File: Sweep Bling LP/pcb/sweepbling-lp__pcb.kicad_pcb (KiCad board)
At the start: 2 copper layers, 216.9 x 86.9 mm, 59 parts, among them SW1 SW_Push, SW10 SW_Push, SW10_r1 SW_Push, SW11 SW_Push, SW11_r1 SW_Push, SW12 SW_Push, SW12_r1 SW_Push, SW13 SW_Push, SW13_r1 SW_Push, SW14 SW_Push, SW14_r1 SW_Push, SW15 SW_Push, SW15_r1 SW_Push, SW16 SW_Push, SW16_r1 SW_Push, SW17 SW_Push, SW17_r1 SW_Push, SW1_r1 SW_Push, SW2 SW_Push, SW2_r1 SW_Push, SW3 SW_Push, SW3_r1 SW_Push, SW4 SW_Push, SW4_r1 SW_Push, SW5 SW_Push, SW5_r1 SW_Push, SW6 SW_Push, SW6_r1 SW_Push, SW7 SW_Push, SW7_r1 SW_Push, SW8 SW_Push, SW8_r1 SW_Push, SW9 SW_Push, SW9_r1 SW_Push, U1 ProMicro-kbd, U2 ProMicro-kbd

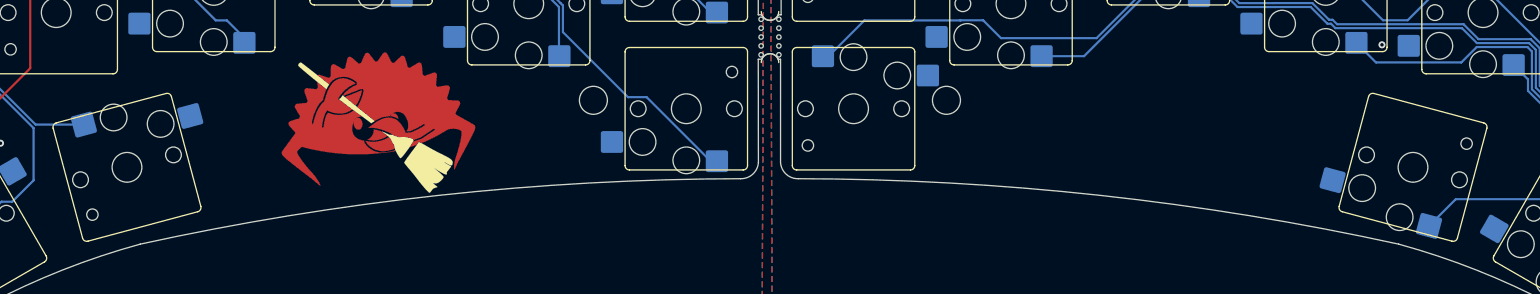
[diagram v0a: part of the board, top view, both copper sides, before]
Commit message: remove crab logo
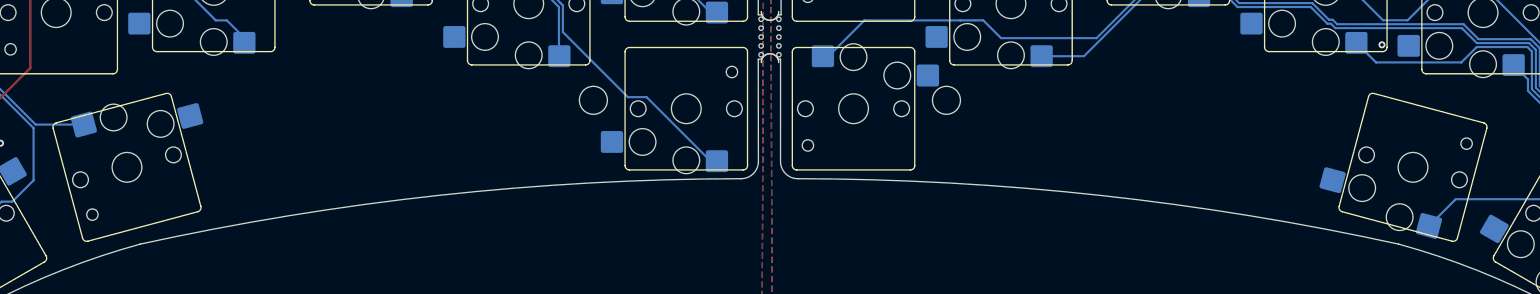
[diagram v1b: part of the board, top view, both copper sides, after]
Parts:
- removed SweepLogo: LOGO, Kailh:ferris_broom

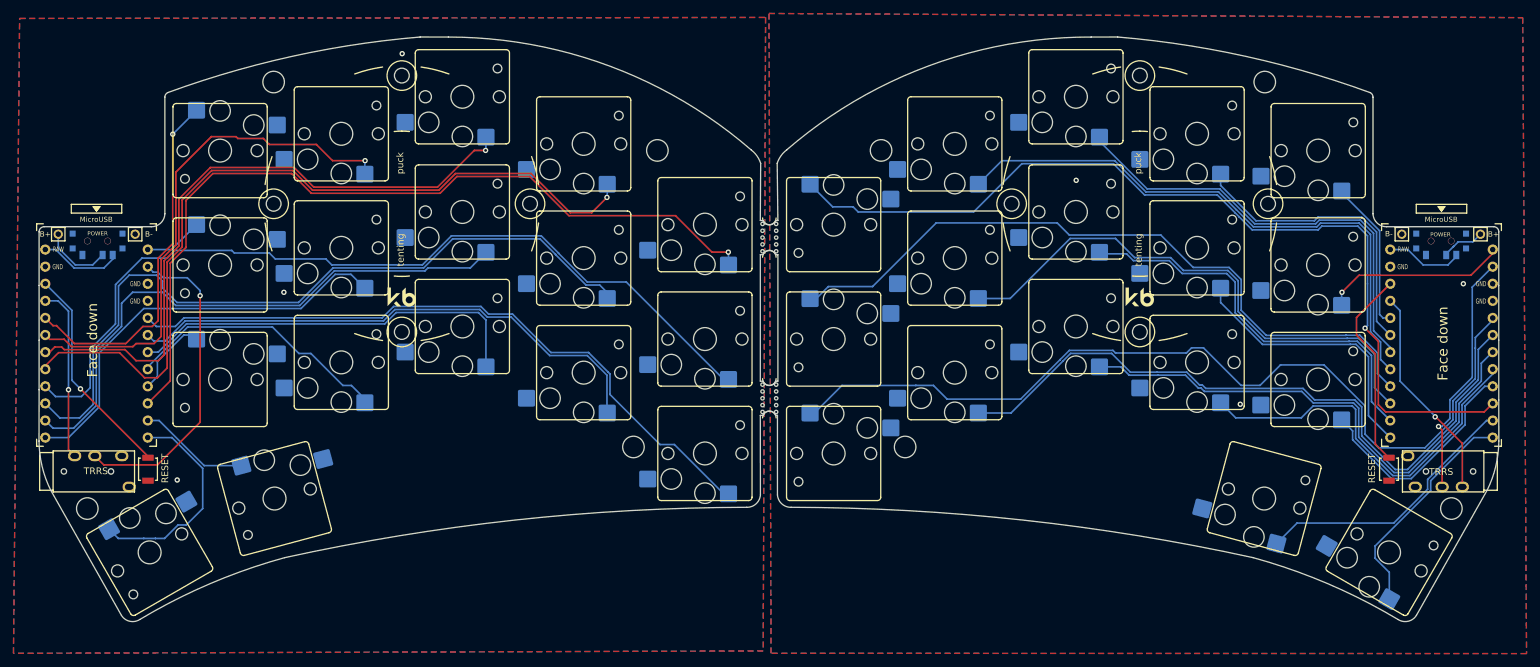
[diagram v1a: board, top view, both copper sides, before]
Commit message: reduce tenting pucks
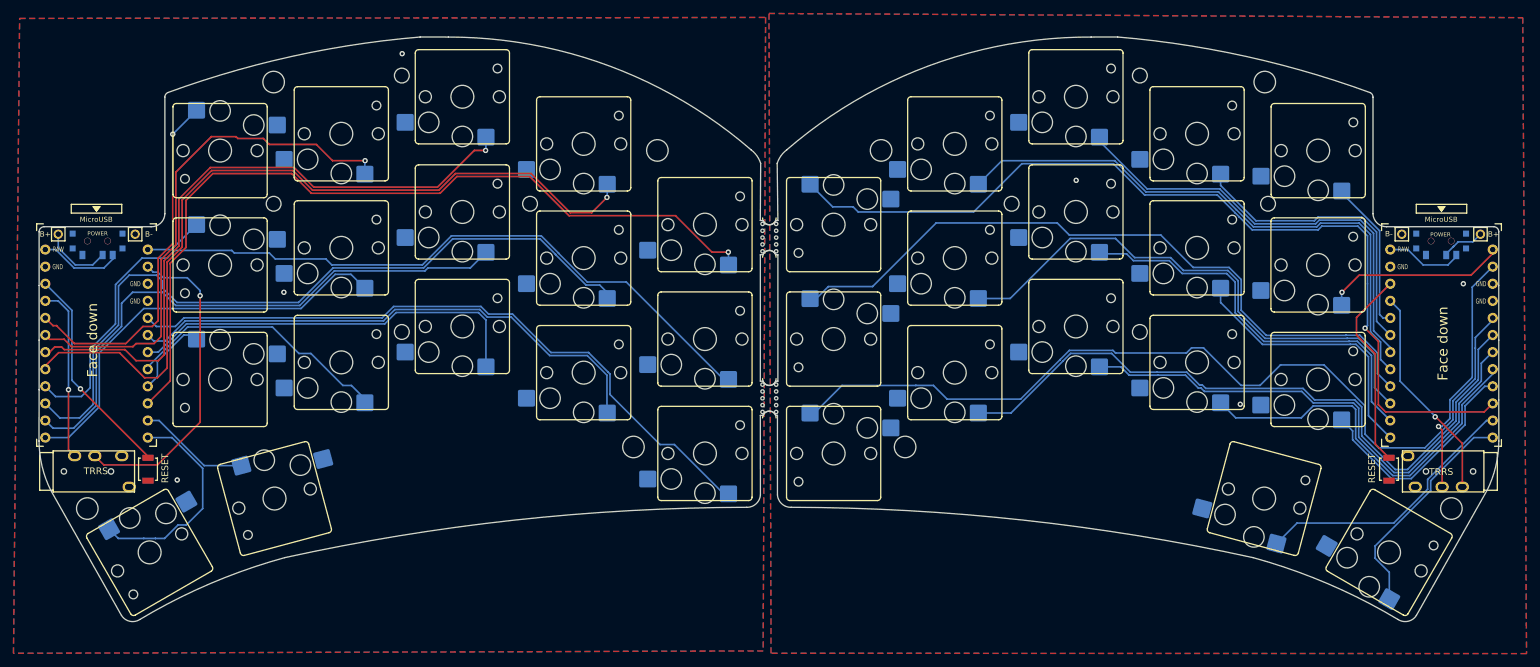
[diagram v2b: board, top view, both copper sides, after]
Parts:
- REF_PUCK_R, e: footprint * duckyb-collection:Tenting_Puck2_no_pads -> scda:Tenting_Puck2_no_pads_no_text

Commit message: remove version silk
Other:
- board text removed: "v1.0"
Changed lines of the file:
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@@
   (gr_line (start 131.5085 77.724) (end 131.2545 77.724) (layer "Edge.Cuts") (width 0.05))
   (gr_arc (start 129.349501 53.848) (mid 130.302 53.203127) (end 131.254499 53.848001) (layer "Edge.Cuts") (width 0.05))
-  (gr_text "v1.0" (at 140.97 39.116) (layer "B.SilkS")
-    (effects (font (size 1.5 1.5) (thickness 0.3)) (justify mirror))
-  )
   (gr_text "Face down" (at 230.378 67.056 90) (layer "F.SilkS")
     (effects (font (size 1.5 1.5) (thickness 0.3)))

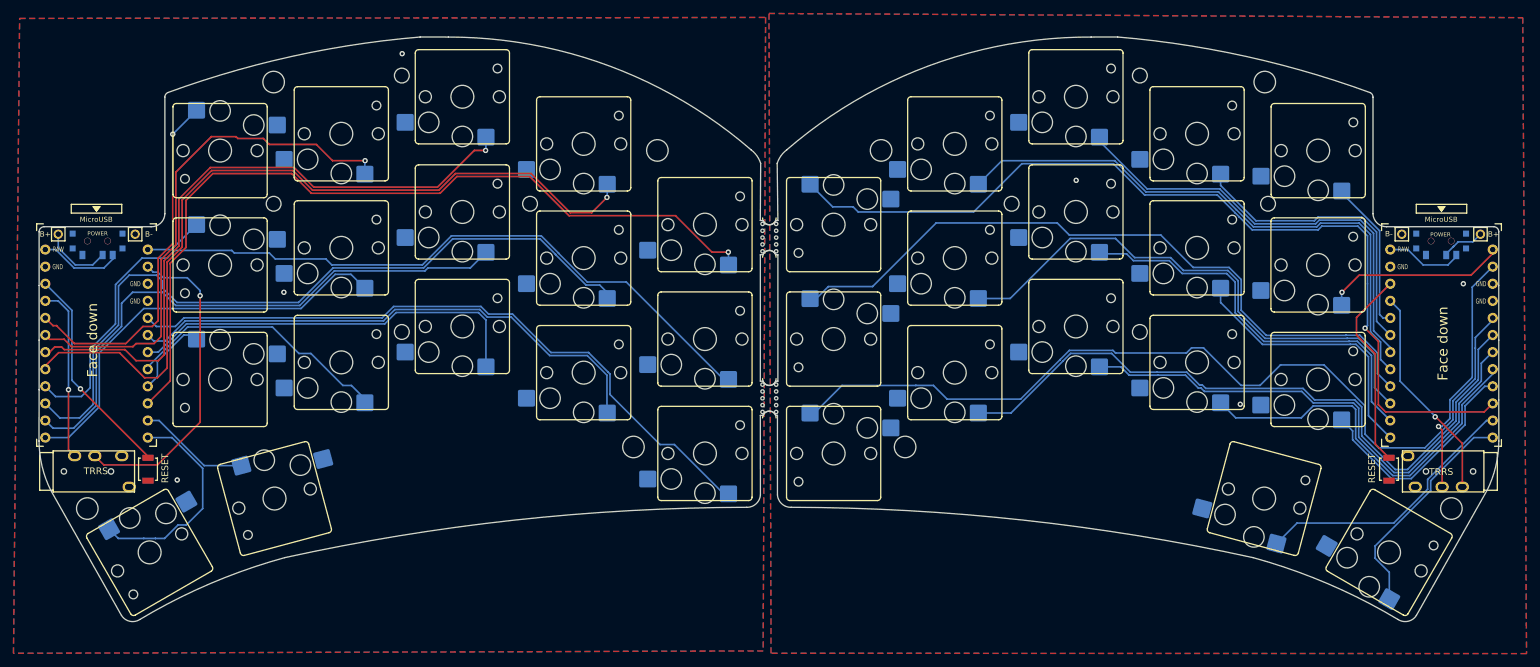
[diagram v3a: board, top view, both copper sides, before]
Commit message: remove trrs ports and connections
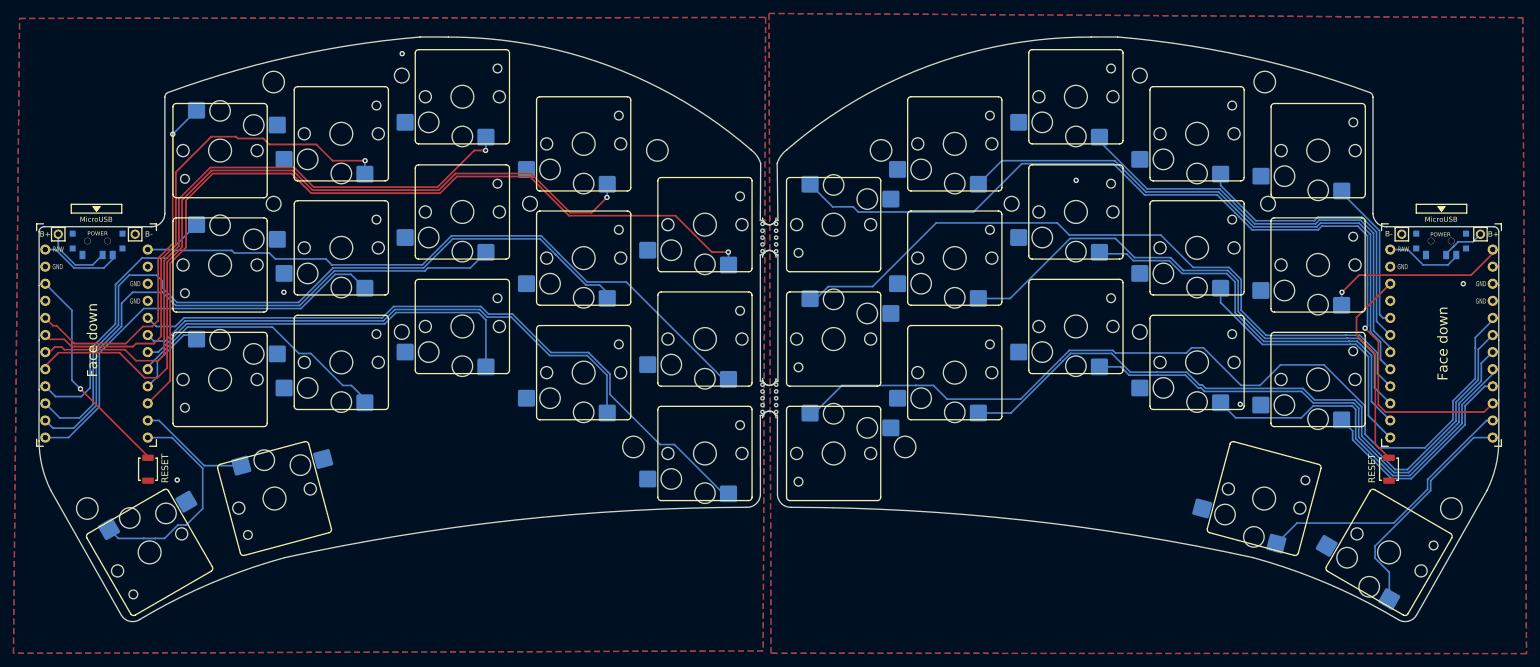
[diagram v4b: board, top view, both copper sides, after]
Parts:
- removed TRRS1, TRRS2: AudioJack4, * duckyb-collection:TRRS-PJ-320A
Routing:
- net Switch18_r: track 47.6 -> 0.00 mm, vias 1 -> 0
- net Switch18: track 36.6 -> 0.00 mm, vias 1 -> 0
- net vcc: track 32.1 -> 0.00 mm, vias 1 -> 0
- net vcc_r: track 26.0 -> 0.00 mm, vias 1 -> 0
